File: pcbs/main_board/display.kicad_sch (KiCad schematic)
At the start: 1 part, among them U4 Display

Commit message: Add reverse polarity protection
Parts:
- U4: footprint display:display_footprint -> Connector_JST:JST_XH_S9B-XH-A-1_1x09_P2.50mm_Horizontal; Manufacturer Part Number LA141073 -> B9B-XH-A-GU; Supplier LaskaKit -> Mouser; Supplier Part Number LA141073 -> 306-B9B-XH-A-GU
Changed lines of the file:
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@@
 			)
 		)
-		(property "Footprint" "display:display_footprint"
+		(property "Footprint" "Connector_JST:JST_XH_S9B-XH-A-1_1x09_P2.50mm_Horizontal"
 			(at 105.41 66.04 0)
 			(effects
@@
 			)
 		)
-		(property "Description" "Display 4 inch"
+		(property "Description" "JST XH 9 pin, female"
 			(at 105.41 66.04 0)
 			(effects
@@
 			)
 		)
-		(property "Manufacturer Part Number" "LA141073"
+		(property "Manufacturer Part Number" "B9B-XH-A-GU"
 			(at 105.41 66.04 0)
 			(effects
@@
 			)
 		)
-		(property "Supplier" "LaskaKit"
+		(property "Supplier" "Mouser"
 			(at 105.41 66.04 0)
 			(effects
@@
 			)
 		)
-		(property "Supplier Part Number" "LA141073"
+		(property "Supplier Part Number" "306-B9B-XH-A-GU"
 			(at 105.41 66.04 0)
 			(effects

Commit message: Add connectors
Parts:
- U4: Manufacturer Part Number B9B-XH-A-GU -> S9B-XH-A-1(LF)(SN); Supplier Part Number 306-B9B-XH-A-GU -> 306-S9BXHA1LFSN
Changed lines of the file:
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@@
 			)
 		)
-		(property "Datasheet" "https://www.lcdwiki.com/4.0inch_SPI_Module_ST7796"
+		(property "Datasheet" "https://cz.mouser.com/datasheet/3/1070/1/eXH.pdf"
 			(at 105.41 66.04 0)
 			(effects
@@
 			)
 		)
-		(property "Description" "JST XH 9 pin, female"
+		(property "Description" "JST XH 9 pin, zásuvka, boční"
 			(at 105.41 66.04 0)
 			(effects
@@
 			)
 		)
-		(property "Manufacturer Part Number" "B9B-XH-A-GU"
+		(property "Manufacturer Part Number" "S9B-XH-A-1(LF)(SN)"
 			(at 105.41 66.04 0)
 			(effects
@@
 			)
 		)
-		(property "Supplier Part Number" "306-B9B-XH-A-GU"
+		(property "Supplier Part Number" "306-S9BXHA1LFSN"
 			(at 105.41 66.04 0)
 			(effects

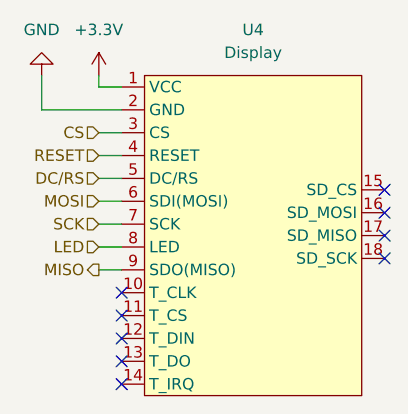
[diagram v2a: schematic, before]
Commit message: Add edge cuts and notes to pcb
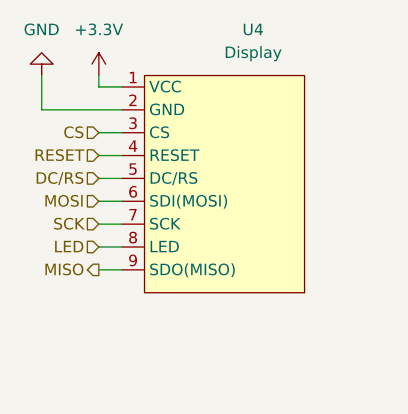
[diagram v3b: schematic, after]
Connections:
- no-connect marks 9 -> 0
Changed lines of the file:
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@@
 	(generator_version "9.0")
 	(paper "A5")
-	(no_connect
-		(at 119.38 62.23)
-	)
-	(no_connect
-		(at 119.38 64.77)
-	)
-	(no_connect
-		(at 119.38 69.85)
-	)
-	(no_connect
-		(at 90.17 83.82)
-	)
-	(no_connect
-		(at 90.17 73.66)
-	)
-	(no_connect
-		(at 90.17 81.28)
-	)
-	(no_connect
-		(at 90.17 78.74)
-	)
-	(no_connect
-		(at 90.17 76.2)
-	)
-	(no_connect
-		(at 119.38 67.31)
-	)
 	(wire
 		(pts
@@
 		(pin "9"
 		)
-		(pin "12"
-		)
-		(pin "14"
-		)
-		(pin "16"
-		)
 		(pin "2"
 		)
@@
 		(pin "8"
 		)
-		(pin "10"
-		)
 		(pin "1"
 		)
@@
 		(pin "7"
 		)
-		(pin "11"
-		)
-		(pin "13"
-		)
-		(pin "15"
-		)
-		(pin "18"
-		)
-		(pin "17"
-		)
 		(instances

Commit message: Components update
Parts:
- U4: footprint Connector_JST:JST_XH_S9B-XH-A-1_1x09_P2.50mm_Horizontal -> Connector_JST:JST_XH_S8B-XH-A-1_1x08_P2.50mm_Horizontal; Manufacturer Part Number S9B-XH-A-1(LF)(SN) -> S8B-XH-A-1 (LF)(SN); Supplier Mouser -> TME; Supplier Part Number 306-S9BXHA1LFSN -> S8B-XH-A-1
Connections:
- removed net MISO: U4.9 (SDO(MISO))
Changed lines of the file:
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@@
-	(wire
-		(pts
-			(xy 87.63 71.12) (xy 90.17 71.12)
-		)
-		(stroke
-			(width 0)
-			(type default)
-		)
-	)
 	(wire
 		(pts
@@
 		(shape input)
 		(at 87.63 58.42 180)
-		(effects
-			(font
-				(size 1.27 1.27)
-			)
-			(justify right)
-		)
-	)
-	(hierarchical_label "MISO"
-		(shape output)
-		(at 87.63 71.12 180)
 		(effects
 			(font
@@
 			)
 		)
-		(property "Footprint" "Connector_JST:JST_XH_S9B-XH-A-1_1x09_P2.50mm_Horizontal"
+		(property "Footprint" "Connector_JST:JST_XH_S8B-XH-A-1_1x08_P2.50mm_Horizontal"
 			(at 105.41 66.04 0)
 			(effects
@@
 			)
 		)
-		(property "Description" "JST XH 9 pin, zásuvka, boční"
-			(at 105.41 66.04 0)
-			(effects
-				(font
-					(size 1.27 1.27)
-				)
-				(hide yes)
-			)
-		)
-		(property "Manufacturer Part Number" "S9B-XH-A-1(LF)(SN)"
-			(at 105.41 66.04 0)
-			(effects
-				(font
-					(size 1.27 1.27)
-				)
-				(hide yes)
-			)
-		)
-		(property "Supplier" "Mouser"
-			(at 105.41 66.04 0)
-			(effects
-				(font
-					(size 1.27 1.27)
-				)
-				(hide yes)
-			)
-		)
-		(property "Supplier Part Number" "306-S9BXHA1LFSN"
+		(property "Description" "JST XH 8 pin, zásuvka, boční"
+			(at 105.41 66.04 0)
+			(effects
+				(font
+					(size 1.27 1.27)
+				)
+				(hide yes)
+			)
+		)
+		(property "Manufacturer Part Number" "S8B-XH-A-1 (LF)(SN)"
+			(at 105.41 66.04 0)
+			(effects
+				(font
+					(size 1.27 1.27)
+				)
+				(hide yes)
+			)
+		)
+		(property "Supplier" "TME"
+			(at 105.41 66.04 0)
+			(effects
+				(font
+					(size 1.27 1.27)
+				)
+				(hide yes)
+			)
+		)
+		(property "Supplier Part Number" "S8B-XH-A-1"
+			(at 105.41 66.04 0)
+			(effects
+				(font
+					(size 1.27 1.27)
+				)
+				(hide yes)
+			)
+		)
+		(property "Mouser number" ""
 			(at 105.41 66.04 0)
 			(effects
@@
 		(pin "4"
 		)
-		(pin "9"
-		)
 		(pin "2"

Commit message: Main board final update
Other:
- company: (none) -> Brno Mars Rover
- title: (none) -> Main board - MyMachine LED cap
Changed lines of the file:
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@@
 	(generator "eeschema")
 	(generator_version "9.0")
-	(paper "A5")
+	(paper "A4")
+	(title_block
+		(title "Main board - MyMachine LED cap")
+		(date "2026-01-20")
+		(company "Brno Mars Rover")
+	)
 	(wire
 		(pts
